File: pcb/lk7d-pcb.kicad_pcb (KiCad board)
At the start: 2 copper layers, 57.2 x 57.2 mm, 32 parts, among them J1 PINHD_1x4_Male, J2 PINHD_1x4_Male, M1 JLCPCB_2DBarcode_5x5mm, SW1 RotaryEncoder_Switch_MP, SW2 RotaryEncoder_Switch_MP, SW3 SW_Push, SW4 SW_Push, SW5 SW_Push, SW6 SW_Push, SW7 SW_Push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

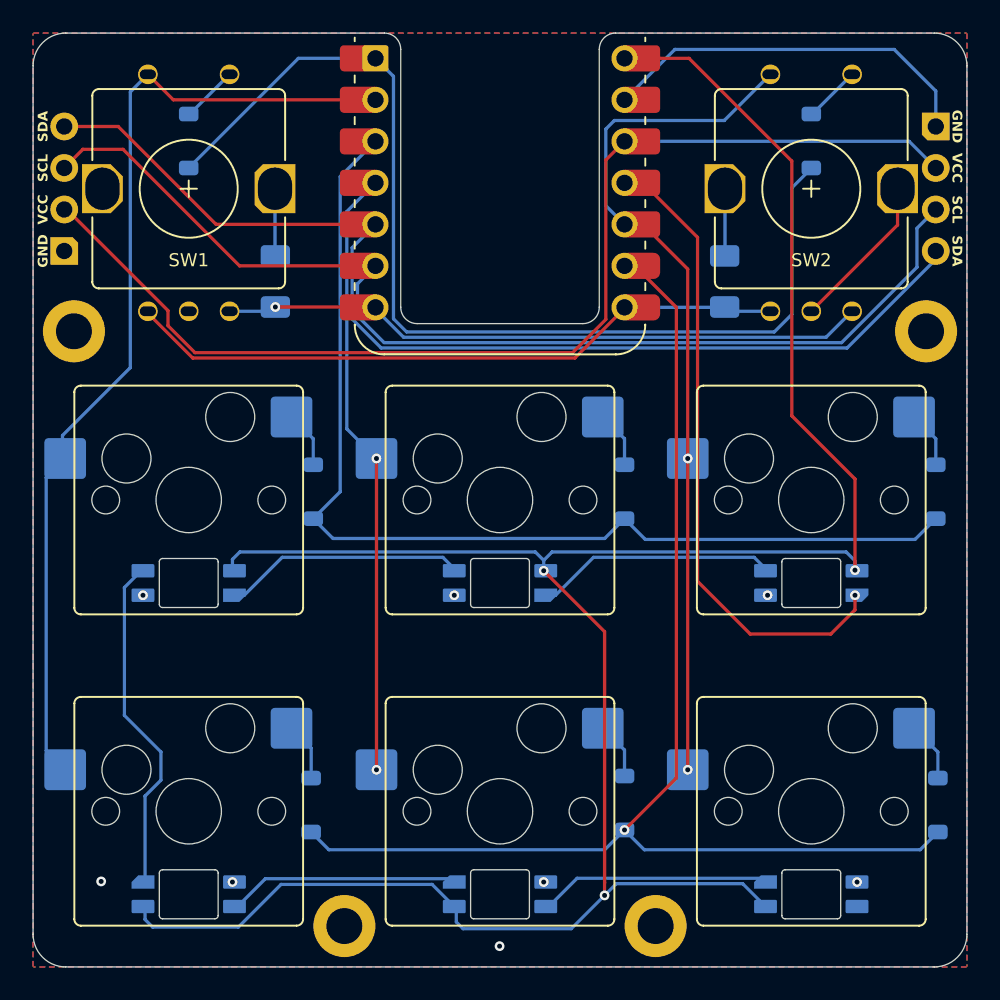
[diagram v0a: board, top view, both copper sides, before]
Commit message: Add Logic Level Converter for per key LEDs (#3)
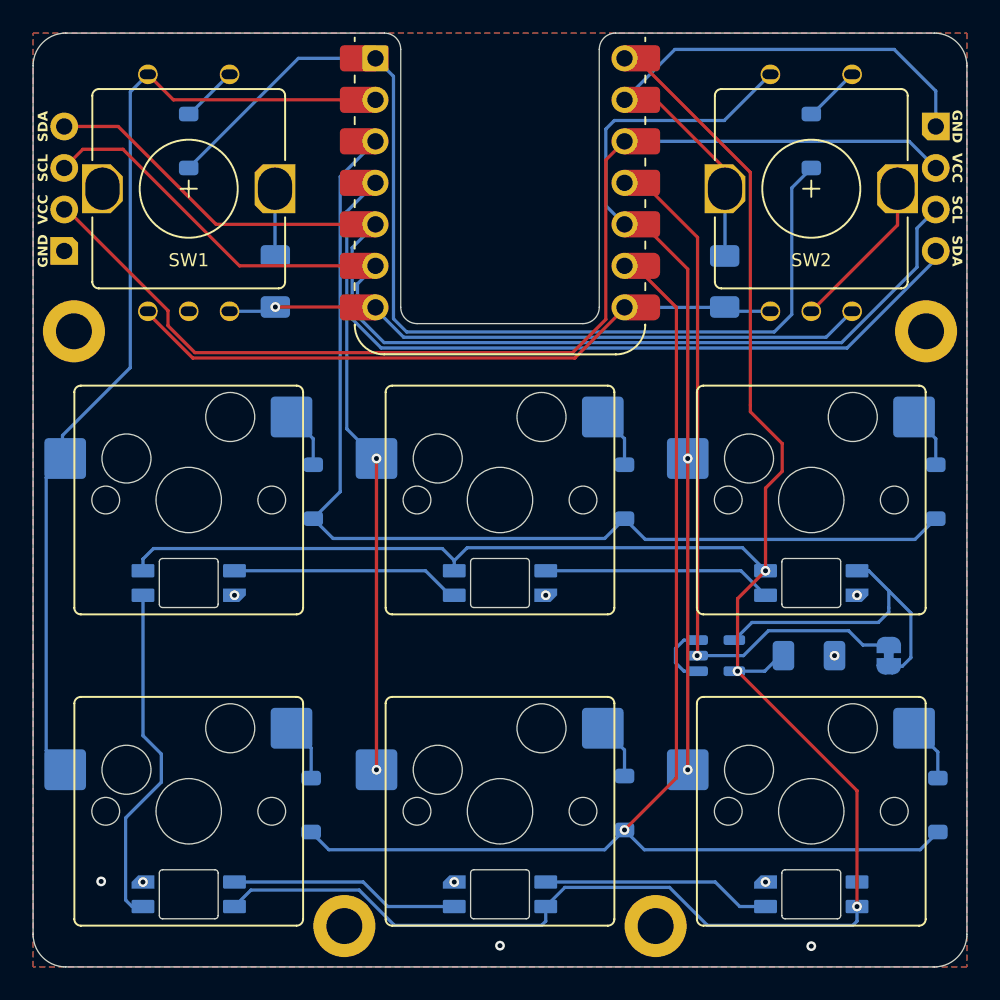
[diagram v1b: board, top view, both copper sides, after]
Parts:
- added C3: 100nF, Capacitor_SMD:C_1206_3216Metric_Pad1.33x1.80mm_HandSolder, B.Cu at (77.5, 68.1)
- added JP1: SolderJumper_2_Bridged, Jumper:SolderJumper-2_P1.3mm_Bridged_RoundedPad1.0x1.5mm, B.Cu at (82.4, 68.1)
- added U2: SN74LV1T125DBV, Package_TO_SOT_SMD:SOT-23-5, B.Cu at (71.8, 68.1)
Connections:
- LED1 pad 1: Net-(LED1-DOUT) -> +5V
- LED1 pad 2: GND -> Net-(LED1-DOUT)
- LED1 pad 3: /LED -> GND
- LED1 pad 4: +5V -> /LEDIN
- LED2 pad 1: Net-(LED2-DOUT) -> +5V
- LED2 pad 2: GND -> Net-(LED2-DOUT)
- LED2 pad 3: Net-(LED1-DOUT) -> GND
- LED2 pad 4: +5V -> Net-(LED1-DOUT)
- LED3 pad 1: Net-(LED3-DOUT) -> +5V
- LED3 pad 2: GND -> Net-(LED3-DOUT)
- LED3 pad 3: Net-(LED2-DOUT) -> GND
- LED3 pad 4: +5V -> Net-(LED2-DOUT)
- LED4 pad 1: Net-(LED4-DOUT) -> +5V
- LED4 pad 2: GND -> Net-(LED4-DOUT)
- LED4 pad 3: Net-(LED3-DOUT) -> GND
- LED4 pad 4: +5V -> Net-(LED3-DOUT)
- LED5 pad 1: Net-(LED5-DOUT) -> +5V
- LED5 pad 2: GND -> Net-(LED5-DOUT)
- LED5 pad 3: Net-(LED4-DOUT) -> GND
- LED5 pad 4: +5V -> Net-(LED4-DOUT)
- LED6 pad 1: unconnected-(LED6-DOUT-Pad1) -> +5V
- LED6 pad 2: GND -> unconnected-(LED6-DOUT-Pad2)
- LED6 pad 3: Net-(LED5-DOUT) -> GND
- LED6 pad 4: +5V -> Net-(LED5-DOUT)
- U1 pad 11: /LED -> /LEDIO
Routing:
- net /LEDIO: track 0.00 -> 44.4 mm, vias 0 -> 1
- net /LED: track 39.4 -> 0.00 mm, vias 1 -> 0
- net /LEDIN: track 0.00 -> 20.8 mm
- net GND: track 41.5 -> 54.0 mm, vias 8 -> 10
- net +5V: track 145.3 -> 147.0 mm
- net Net-(LED2-DOUT): track 15.0 -> 14.1 mm
- net Net-(LED1-DOUT): track 15.0 -> 14.1 mm
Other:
- board text added: "LEDs run on 3.3V logic by default. If your LEDS require 5V logic, cut JP1 and populate U2 and C3."
- board text added: "LK7D v1.01"
- board text removed: "LK7D v1.00"
